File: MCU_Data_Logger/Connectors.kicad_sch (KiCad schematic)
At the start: 4 parts, among them J1 Conn_01x04_Pin, J2 Conn_01x04_Pin, J3 Conn_01x09_Pin, J4 Conn_02x03_Odd_Even

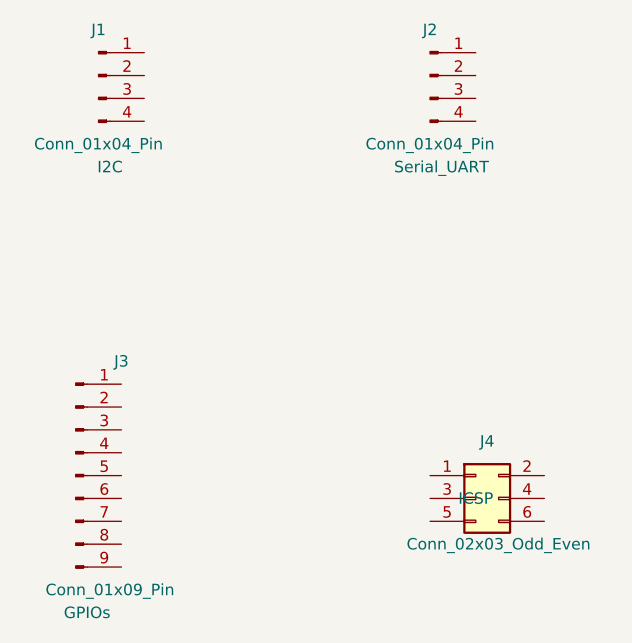
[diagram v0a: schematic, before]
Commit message: finlize sch wiring
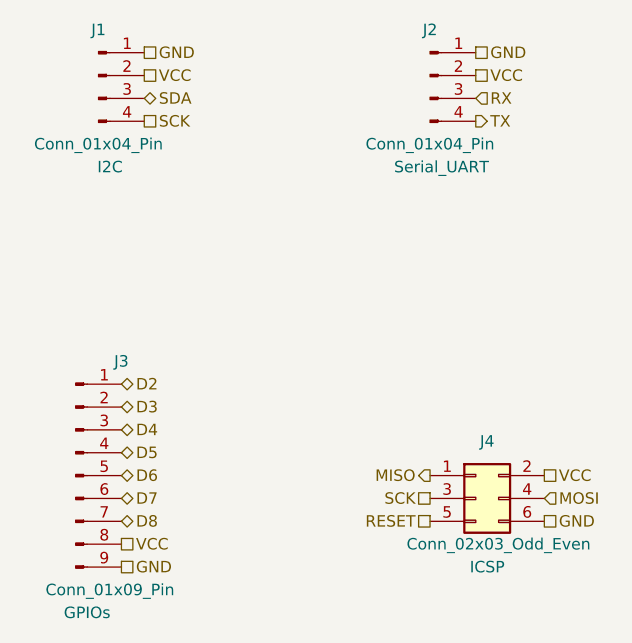
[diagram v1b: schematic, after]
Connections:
- net MISO: now reaches J4.1 (Pin_1)
- net VCC: now reaches J4.2 (Pin_2)
- net VCC: now also J1.2 (Pin_2), J2.2 (Pin_2), J3.8 (Pin_8)
- net SCK: now reaches J4.3 (Pin_3)
- net SCK: now also J1.4 (Pin_4)
- net MOSI: now reaches J4.4 (Pin_4)
- net RESET: now reaches J4.5 (Pin_5)
- net GND: now reaches J4.6 (Pin_6)
- net GND: now also J1.1 (Pin_1), J2.1 (Pin_1), J3.9 (Pin_9)
- net SDA: now reaches J1.3 (Pin_3)
- net D2: now reaches J3.1 (Pin_1)
- net D3: now reaches J3.2 (Pin_2)
- net D4: now reaches J3.3 (Pin_3)
- net D5: now reaches J3.4 (Pin_4)
- net D6: now reaches J3.5 (Pin_5)
- net D7: now reaches J3.6 (Pin_6)
- net D8: now reaches J3.7 (Pin_7)
- net RX: now reaches J2.3 (Pin_3)
- net TX: now reaches J2.4 (Pin_4)
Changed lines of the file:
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@@
 		(rev "V1")
+	)
+	(hierarchical_label "GND"
+		(shape passive)
+		(at 181.61 72.39 0)
+		(effects
+			(font
+				(size 1.27 1.27)
+			)
+			(justify left)
+		)
+	)
+	(hierarchical_label "D6"
+		(shape bidirectional)
+		(at 142.24 119.38 0)
+		(effects
+			(font
+				(size 1.27 1.27)
+			)
+			(justify left)
+		)
+	)
+	(hierarchical_label "D5"
+		(shape bidirectional)
+		(at 142.24 116.84 0)
+		(effects
+			(font
+				(size 1.27 1.27)
+			)
+			(justify left)
+		)
+	)
+	(hierarchical_label "D2"
+		(shape bidirectional)
+		(at 142.24 109.22 0)
+		(effects
+			(font
+				(size 1.27 1.27)
+			)
+			(justify left)
+		)
+	)
+	(hierarchical_label "GND"
+		(shape passive)
+		(at 142.24 129.54 0)
+		(effects
+			(font
+				(size 1.27 1.27)
+			)
+			(justify left)
+		)
+	)
+	(hierarchical_label "TX"
+		(shape output)
+		(at 181.61 80.01 0)
+		(effects
+			(font
+				(size 1.27 1.27)
+			)
+			(justify left)
+		)
+	)
+	(hierarchical_label "GND"
+		(shape passive)
+		(at 144.78 72.39 0)
+		(effects
+			(font
+				(size 1.27 1.27)
+			)
+			(justify left)
+		)
+	)
+	(hierarchical_label "VCC"
+		(shape passive)
+		(at 142.24 127 0)
+		(effects
+			(font
+				(size 1.27 1.27)
+			)
+			(justify left)
+		)
+	)
+	(hierarchical_label "D7"
+		(shape bidirectional)
+		(at 142.24 121.92 0)
+		(effects
+			(font
+				(size 1.27 1.27)
+			)
+			(justify left)
+		)
+	)
+	(hierarchical_label "D8"
+		(shape bidirectional)
+		(at 142.24 124.46 0)
+		(effects
+			(font
+				(size 1.27 1.27)
+			)
+			(justify left)
+		)
+	)
+	(hierarchical_label "VCC"
+		(shape passive)
+		(at 144.78 74.93 0)
+		(effects
+			(font
+				(size 1.27 1.27)
+			)
+			(justify left)
+		)
+	)
+	(hierarchical_label "D4"
+		(shape bidirectional)
+		(at 142.24 114.3 0)
+		(effects
+			(font
+				(size 1.27 1.27)
+			)
+			(justify left)
+		)
+	)
+	(hierarchical_label "SCK"
+		(shape passive)
+		(at 176.53 121.92 180)
+		(effects
+			(font
+				(size 1.27 1.27)
+			)
+			(justify right)
+		)
+	)
+	(hierarchical_label "MISO"
+		(shape output)
+		(at 176.53 119.38 180)
+		(effects
+			(font
+				(size 1.27 1.27)
+			)
+			(justify right)
+		)
+	)
+	(hierarchical_label "GND"
+		(shape passive)
+		(at 189.23 124.46 0)
+		(effects
+			(font
+				(size 1.27 1.27)
+			)
+			(justify left)
+		)
+	)
+	(hierarchical_label "SDA"
+		(shape bidirectional)
+		(at 144.78 77.47 0)
+		(effects
+			(font
+				(size 1.27 1.27)
+			)
+			(justify left)
+		)
+	)
+	(hierarchical_label "MOSI"
+		(shape input)
+		(at 189.23 121.92 0)
+		(effects
+			(font
+				(size 1.27 1.27)
+			)
+			(justify left)
+		)
+	)
+	(hierarchical_label "VCC"
+		(shape passive)
+		(at 189.23 119.38 0)
+		(effects
+			(font
+				(size 1.27 1.27)
+			)
+			(justify left)
+		)
+	)
+	(hierarchical_label "VCC"
+		(shape passive)
+		(at 181.61 74.93 0)
+		(effects
+			(font
+				(size 1.27 1.27)
+			)
+			(justify left)
+		)
+	)
+	(hierarchical_label "RX"
+		(shape input)
+		(at 181.61 77.47 0)
+		(effects
+			(font
+				(size 1.27 1.27)
+			)
+			(justify left)
+		)
+	)
+	(hierarchical_label "SCK"
+		(shape passive)
+		(at 144.78 80.01 0)
+		(effects
+			(font
+				(size 1.27 1.27)
+			)
+			(justify left)
+		)
+	)
+	(hierarchical_label "D3"
+		(shape bidirectional)
+		(at 142.24 111.76 0)
+		(effects
+			(font
+				(size 1.27 1.27)
+			)
+			(justify left)
+		)
+	)
+	(hierarchical_label "RESET"
+		(shape passive)
+		(at 176.53 124.46 180)
+		(effects
+			(font
+				(size 1.27 1.27)
+			)
+			(justify right)
+		)
 	)
 	(symbol
@@
 		)
 		(property "Purpose" "ICSP"
-			(at 181.61 121.92 0)
-			(effects
-				(font
+			(at 182.88 129.54 0)
+			(effects
+				(font
